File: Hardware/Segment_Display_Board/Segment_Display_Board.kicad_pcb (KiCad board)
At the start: 2 copper layers, 64.4 x 141 mm, 83 parts, among them J101 IN, J102 OUT, J301 USB_B_Micro, J302 PROG, J401 19V Input, J501 Bottom Conn, J502 Top Conn, Q1001 MMBT3904, Q1002 MMBT3906, Q1101 MMBT3904, Q1102 MMBT3906, Q1201 MMBT3904, Q1202 MMBT3906, Q601 MMBT3904, Q602 MMBT3906, Q701 MMBT3904, Q702 MMBT3906, Q801 MMBT3904, Q802 MMBT3906, Q901 MMBT3904, Q902 MMBT3906, SW201 RESET, SW202 DAY_RESET, SW203 DAY_ADV, SW204 DAY_SUB, U201 ATmega328P-A, U202 DS1307Z+, U301 FT232RL, U401 LM1117-5.0, U501 SN74HC595, Y201 16mHz, Y202 32.768kHz

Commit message: Steps for a RC1
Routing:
- net /USB/USB+: track 13.1 -> 15.1 mm
- net /USB/USB-: track 14.3 -> 15.2 mm

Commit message: Fix stuff i guess goodnight"
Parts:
- added JP501: SolderJumper_2_Bridged, Jumper:SolderJumper-2_P1.3mm_Bridged_Pad1.0x1.5mm, B.Cu at (166.5, 131.0)
- added JP502: SolderJumper_2_Bridged, Jumper:SolderJumper-2_P1.3mm_Bridged_Pad1.0x1.5mm, B.Cu at (166.5, 128.5)
- moved C303 0.50 mm to (121.5, 111.5)
- moved D302 0.25 mm to (115.0, 122.2)
- moved R302 0.25 mm to (118.5, 122.2)
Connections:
- net +3V3 renamed +3.3V
- J102 pad 3: /C_OUT -> /Display Card/CLOCK_OUT
- J102 pad 4: /L_OUT -> /Display Card/LATCH_OUT
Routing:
- net /L_OUT: track 99.1 -> 92.1 mm
- net /Display Card/LATCH_OUT: track 0.00 -> 6.40 mm
- net /Display Card/CLOCK_OUT: track 0.00 -> 6.36 mm
- net /C_OUT: track 92.7 -> 86.4 mm
- net VBUS: track 10.5 -> 10.00 mm
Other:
- board text added: "LCD Display Card ${FULL_REVISION}"
- board text removed: "LCD Display Card ${FULL_VERSION}"

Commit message: Add a bunch more great stuff
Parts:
- added G***: LOGO, 1721_templates:QRCODE_AccidentCounter, F.Cu at (122.5, 158.2)
- added REF**: OSHW-Symbol_13.4x12mm_SilkScreen, Symbol:OSHW-Symbol_13.4x12mm_SilkScreen, F.Cu at (124.2, 73.5)
- moved G*** 97.7 mm to (124.2, 59.0)
- moved D301 89.6 mm to (119.0, 35.0)
- moved D302 89.6 mm to (119.0, 32.8)
- moved R301 89.6 mm to (122.5, 35.0)
- moved R302 89.6 mm to (122.5, 32.8)
- moved C301 88.2 mm to (117.2, 40.0), turned to 180 degrees
- moved J301 83.5 mm to (131.2, 32.1), turned to 180 degrees
- moved C302 77.6 mm to (139.8, 32.0), turned to 0 degrees
- moved U301 77.5 mm to (124.2, 43.5), turned to 180 degrees
- moved C303 74.0 mm to (133.8, 38.5), turned to 0 degrees
- moved BT201 44.1 mm to (161.8, 50.5), turned to 90 degrees
- moved R205 30.6 mm to (144.8, 45.0), turned to 0 degrees
- moved R204 29.8 mm to (144.8, 43.0), turned to 0 degrees
- moved U202 28.2 mm to (140.8, 49.0), turned to 0 degrees
- moved Y202 28.2 mm to (144.2, 39.0), turned to 180 degrees
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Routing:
- net /MCU/RXD: track 14.7 -> 80.8 mm, vias 2 -> 3
- net /MCU/TXD: track 12.3 -> 77.5 mm
- net Net-(C304-Pad2): track 9.15 -> 73.1 mm
- net Net-(BT201-Pad1): track 36.4 -> 51.5 mm, vias 2 -> 4
- net +5V: track 303.3 -> 291.0 mm
- net +19V: track 215.8 -> 209.5 mm
- net /L_OUT: track 92.1 -> 86.1 mm
- net /D_OUT: track 82.8 -> 76.8 mm
- net /C_OUT: track 86.4 -> 80.3 mm
- net /MCU/SDA: track 72.7 -> 78.2 mm
- net /MCU/DAY_SUBTRACT: track 48.7 -> 54.2 mm
- net /MCU/DAY_ADVANCE: track 57.6 -> 63.0 mm
- net /MCU/DAY_RESET: track 64.6 -> 70.0 mm
- net GND: track 27.7 -> 22.9 mm
- net Net-(R302-Pad2): track 10.4 -> 14.3 mm
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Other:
- board size 64.4 x 141 mm -> 58.4 x 141 mm
- board text added: "Designed for FRC 1721 Tidal Force By Joe and Mark Sedutto"

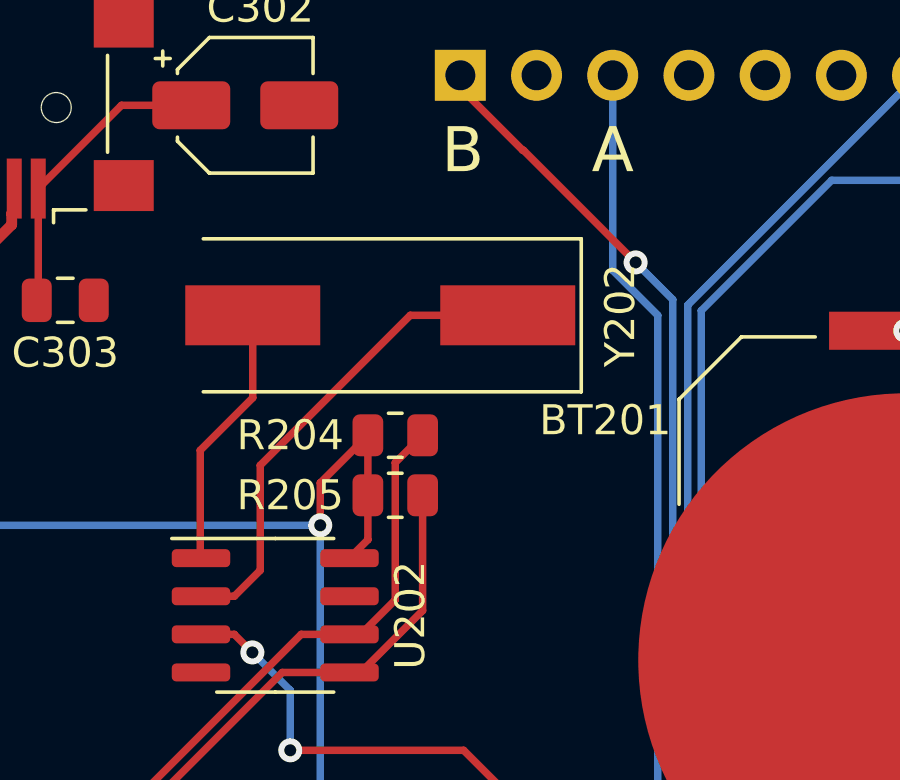
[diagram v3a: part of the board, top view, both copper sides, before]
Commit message: Place hardware orders
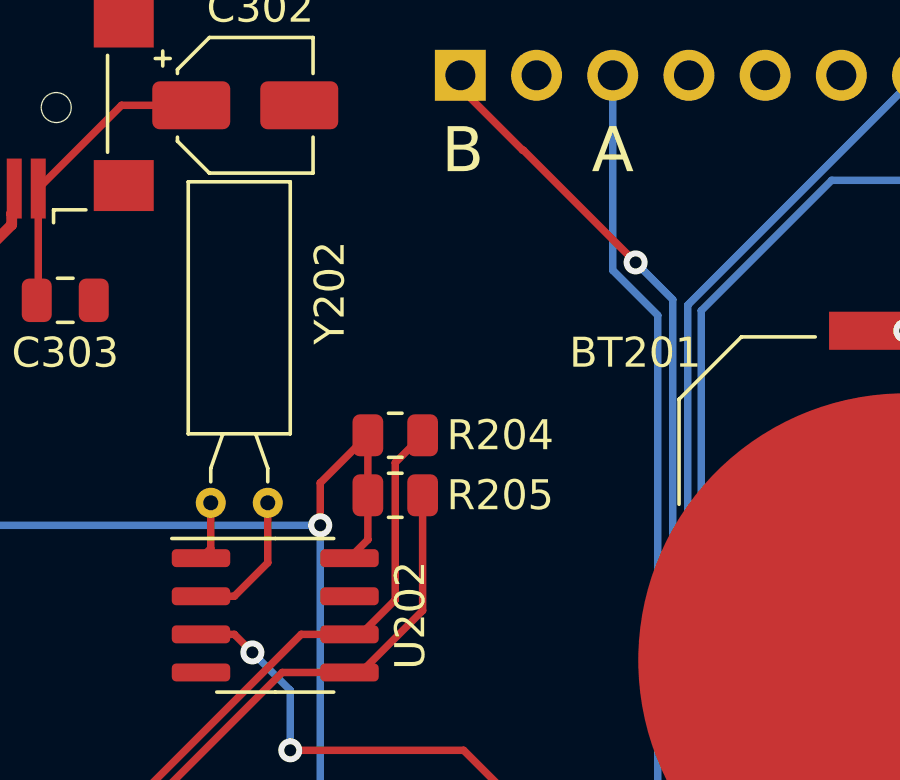
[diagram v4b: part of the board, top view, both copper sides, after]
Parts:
- R1003, R1103, R1203, R603, R703, R803, R903: value 250R -> 240R
- Y202: footprint Crystal:Crystal_SMD_HC49-SD -> Crystal:Crystal_C38-LF_D3.0mm_L8.0mm_Horizontal
- moved Y202 7.29 mm to (140.5, 45.2)
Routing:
- net Net-(U202-Pad2): track 16.2 -> 4.69 mm
- net Net-(U202-Pad1): track 8.83 -> 2.01 mm
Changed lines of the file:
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@@
       (effects (font (size 1 1) (thickness 0.15)))
     )
-    (fp_text value "4.7uf" (at 0 3.2) (layer "F.Fab")
+    (fp_text value "4.7uf" (at 4.5 1.75) (layer "F.Fab")
       (effects (font (size 1 1) (thickness 0.15)))
     )
@@
     (property "Sheetname" "MCU")
     (attr smd)
-    (fp_text reference "BT201" (at 8 -10) (layer "F.SilkS")
+    (fp_text reference "BT201" (at 10.25 -9) (layer "F.SilkS")
       (effects (font (size 1 1) (thickness 0.15)))
     )
@@
       (effects (font (size 0.75 0.75) (thickness 0.15)))
     )
-    (fp_text value "250R" (at 0 2.5) (layer "F.Fab")
+    (fp_text value "240R" (at 0 2.5) (layer "F.Fab")
       (effects (font (size 1 1) (thickness 0.15)))
     )
@@
     (property "Sheetname" "MCU")
     (attr smd)
-    (fp_text reference "R204" (at -3.5 0) (layer "F.SilkS")
+    (fp_text reference "R204" (at 3.5 0) (layer "F.SilkS")
       (effects (font (size 1 1) (thickness 0.15)))
     )
@@
       (effects (font (size 0.75 0.75) (thickness 0.15)))
     )
-    (fp_text value "250R" (at 0 2.5) (layer "F.Fab")
+    (fp_text value "240R" (at 0 2.5) (layer "F.Fab")
       (effects (font (size 1 1) (thickness 0.15)))
     )
@@
       (effects (font (size 0.75 0.75) (thickness 0.15)))
     )
-    (fp_text value "250R" (at 0 2.5) (layer "F.Fab")
+    (fp_text value "240R" (at 0 2.5) (layer "F.Fab")
       (effects (font (size 1 1) (thickness 0.15)))
     )
@@
       (effects (font (size 0.75 0.75) (thickness 0.15)))
     )
-    (fp_text value "250R" (at 0 2.5) (layer "F.Fab")
+    (fp_text value "240R" (at 0 2.5) (layer "F.Fab")
       (effects (font (size 1 1) (thickness 0.15)))
     )
@@
     (property "Sheetname" "MCU")
     (attr smd)
-    (fp_text reference "R205" (at -3.5 0) (layer "F.SilkS")
+    (fp_text reference "R205" (at 3.5 0) (layer "F.SilkS")
       (effects (font (size 1 1) (thickness 0.15)))
     )
@@
       (effects (font (size 0.75 0.75) (thickness 0.15)))
     )
-    (fp_text value "250R" (at 0 2.5) (layer "F.Fab")
+    (fp_text value "240R" (at 0 2.5) (layer "F.Fab")
       (effects (font (size 1 1) (thickness 0.15)))
     )
@@
       (effects (font (size 0.75 0.75) (thickness 0.15)))
     )
-    (fp_text value "250R" (at 0 2.5) (layer "F.Fab")
+    (fp_text value "240R" (at 0 2.5) (layer "F.Fab")
       (effects (font (size 1 1) (thickness 0.15)))
     )
@@
     )
   )
-  (footprint "Crystal:Crystal_SMD_HC49-SD" (layer "F.Cu")
-    (at 144.25 39 180)
-    (descr "SMD Crystal HC-49-SD http://cdn-reichelt.de/documents/datenblatt/B400/xxx-HC49-SMD.pdf, 11.4x4.7mm^2 package")
-    (tags "SMD SMT crystal")
+  (footprint "Crystal:Crystal_C38-LF_D3.0mm_L8.0mm_Horizontal" (layer "F.Cu")
+    (at 140.5 45.25 180)
+    (descr "Crystal THT C38-LF 8.0mm length 3.0mm diameter")
+    (tags "['C38-LF']")
     (property "Sheetfile" "mcu.kicad_sch")
     (property "Sheetname" "MCU")
-    (attr smd)
-    (fp_text reference "Y202" (at -8 0 90) (layer "F.SilkS")
+    (attr through_hole)
+    (fp_text reference "Y202" (at -2.07 7 270) (layer "F.SilkS")
       (effects (font (size 1 1) (thickness 0.15)))
     )
-    (fp_text value "32.768kHz" (at -1.75 3.25) (layer "F.Fab")
+    (fp_text value "32.768kHz" (at 1 6.5 270) (layer "F.Fab")
       (effects (font (size 1 1) (thickness 0.15)))
     )
-    (fp_text user "${REFERENCE}" (at 0 0) (layer "F.Fab")
-      (effects (font (size 1 1) (thickness 0.15)))
+    (fp_text user "${REFERENCE}" (at 1.25 6.5 270) (layer "F.Fab")
+      (effects (font (size 0.7 0.7) (thickness 0.105)))
     )
-    (fp_line (start -6.7 2.55) (end 5.9 2.55) (layer "F.SilkS") (width 0.12))
-    (fp_line (start -6.7 -2.55) (end -6.7 2.55) (layer "F.SilkS") (width 0.12))
-    (fp_line (start 5.9 -2.55) (end -6.7 -2.55) (layer "F.SilkS") (width 0.12))
-    (fp_line (start -6.8 2.6) (end 6.8 2.6) (layer "F.CrtYd") (width 0.05))
-    (fp_line (start -6.8 -2.6) (end -6.8 2.6) (layer "F.CrtYd") (width 0.05))
-    (fp_line (start 6.8 2.6) (end 6.8 -2.6) (layer "F.CrtYd") (width 0.05))
-    (fp_line (start 6.8 -2.6) (end -6.8 -2.6) (layer "F.CrtYd") (width 0.05))
-    (fp_line (start -3.015 2.115) (end 3.015 2.115) (layer "F.Fab") (width 0.1))
-    (fp_line (start 5.7 2.35) (end 5.7 -2.35) (layer "F.Fab") (width 0.1))
-    (fp_line (start -5.7 2.35) (end 5.7 2.35) (layer "F.Fab") (width 0.1))
-    (fp_line (start -5.7 -2.35) (end -5.7 2.35) (layer "F.Fab") (width 0.1))
-    (fp_line (start -3.015 -2.115) (end 3.015 -2.115) (layer "F.Fab") (width 0.1))
-    (fp_line (start 5.7 -2.35) (end -5.7 -2.35) (layer "F.Fab") (width 0.1))
-    (fp_arc (start 3.015 -2.115) (mid 5.13 0) (end 3.015 2.115) (layer "F.Fab") (width 0.1))
-    (fp_arc (start -3.015 2.115) (mid -5.13 0) (end -3.015 -2.115) (layer "F.Fab") (width 0.1))
-    (pad "1" smd rect (at -4.25 0 180) (size 4.5 2) (layers "F.Cu" "F.Paste" "F.Mask")
+    (fp_line (start -0.75 2.3) (end -0.75 10.7) (layer "F.SilkS") (width 0.12))
+    (fp_line (start 1.495 2.3) (end 1.9 1.15) (layer "F.SilkS") (width 0.12))
+    (fp_line (start 2.65 10.7) (end 2.65 2.3) (layer "F.SilkS") (width 0.12))
+    (fp_line (start 0.405 2.3) (end 0 1.15) (layer "F.SilkS") (width 0.12))
+    (fp_line (start 2.65 2.3) (end -0.75 2.3) (layer "F.SilkS") (width 0.12))
+    (fp_line (start 1.9 1.15) (end 1.9 0.7) (layer "F.SilkS") (width 0.12))
+    (fp_line (start 0 1.15) (end 0 0.7) (layer "F.SilkS") (width 0.12))
+    (fp_line (start -0.75 10.7) (end 2.65 10.7) (layer "F.SilkS") (width 0.12))
+    (fp_line (start 3.2 11.3) (end 3.2 -0.8) (layer "F.CrtYd") (width 0.05))
+    (fp_line (start -1.3 -0.8) (end -1.3 11.3) (layer "F.CrtYd") (width 0.05))
+    (fp_line (start 3.2 -0.8) (end -1.3 -0.8) (layer "F.CrtYd") (width 0.05))
+    (fp_line (start -1.3 11.3) (end 3.2 11.3) (layer "F.CrtYd") (width 0.05))
+    (fp_line (start 1.9 1.25) (end 1.9 0) (layer "F.Fab") (width 0.1))
+    (fp_line (start 0 1.25) (end 0 0) (layer "F.Fab") (width 0.1))
+    (fp_line (start 1.495 2.5) (end 1.9 1.25) (layer "F.Fab") (width 0.1))
+    (fp_line (start 2.45 2.5) (end -0.55 2.5) (layer "F.Fab") (width 0.1))
+    (fp_line (start -0.55 10.5) (end 2.45 10.5) (layer "F.Fab") (width 0.1))
+    (fp_line (start 0.405 2.5) (end 0 1.25) (layer "F.Fab") (width 0.1))
+    (fp_line (start -0.55 2.5) (end -0.55 10.5) (layer "F.Fab") (width 0.1))
+    (fp_line (start 2.45 10.5) (end 2.45 2.5) (layer "F.Fab") (width 0.1))
+    (pad "1" thru_hole circle (at 0 0 180) (size 1 1) (drill 0.5) (layers *.Cu *.Mask)
       (net 66 "Net-(U202-Pad2)") (pinfunction "1") (pintype "passive"))
-    (pad "2" smd rect (at 4.25 0 180) (size 4.5 2) (layers "F.Cu" "F.Paste" "F.Mask")
+    (pad "2" thru_hole circle (at 1.9 0 180) (size 1 1) (drill 0.5) (layers *.Cu *.Mask)
       (net 65 "Net-(U202-Pad1)") (pinfunction "2") (pintype "passive"))
-    (model "${KICAD6_3DMODEL_DIR}/Crystal.3dshapes/Crystal_SMD_HC49-SD.wrl"
+    (model "${KICAD6_3DMODEL_DIR}/Crystal.3dshapes/Crystal_C38-LF_D3.0mm_L8.0mm_Horizontal.wrl"
       (offset (xyz 0 0 0))
       (scale (xyz 1 1 1))
@@
       (effects (font (size 0.75 0.75) (thickness 0.15)))
     )
-    (fp_text value "250R" (at 0 2.5) (layer "F.Fab")
+    (fp_text value "240R" (at 0 2.5) (layer "F.Fab")
       (effects (font (size 1 1) (thickness 0.15)))
     )
@@
   (segment (start 133.5 108) (end 133.5 104.5) (width 0.25) (layer "F.Cu") (net 64))
   (segment (start 143.601751 50.905) (end 143.225 50.905) (width 0.25) (layer "F.Cu") (net 64))
-  (segment (start 140 41.75) (end 138.25 43.5) (width 0.25) (layer "F.Cu") (net 65))
   (segment (start 138.25 47.07) (end 138.275 47.095) (width 0.25) (layer "F.Cu") (net 65))
-  (segment (start 140 39) (end 140 41.75) (width 0.25) (layer "F.Cu") (net 65))
-  (segment (start 138.25 43.5) (end 138.25 47.07) (width 0.25) (layer "F.Cu") (net 65))
-  (segment (start 140.25 47.5) (end 140.25 44) (width 0.25) (layer "F.Cu") (net 66))
-  (segment (start 140.25 44) (end 145.25 39) (width 0.25) (layer "F.Cu") (net 66))
-  (segment (start 138.275 48.365) (end 139.385 48.365) (width 0.25) (layer "F.Cu") (net 66))
-  (segment (start 139.385 48.365) (end 140.25 47.5) (width 0.25) (layer "F.Cu") (net 66))
-  (segment (start 145.25 39) (end 148.5 39) (width 0.25) (layer "F.Cu") (net 66))
+  (segment (start 138.6 46.77) (end 138.6 45.25) (width 0.25) (layer "F.Cu") (net 65))
+  (segment (start 138.275 47.095) (end 138.6 46.77) (width 0.25) (layer "F.Cu") (net 65))
+  (segment (start 140.5 45.25) (end 140.5 47.25) (width 0.25) (layer "F.Cu") (net 66))
+  (segment (start 139.385 48.365) (end 138.275 48.365) (width 0.25) (layer "F.Cu") (net 66))
+  (segment (start 140.5 47.25) (end 139.385 48.365) (width 0.25) (layer "F.Cu") (net 66))
   (segment (start 124.5 106.38) (end 126.93 106.38) (width 0.25) (layer "F.Cu") (net 69))
   (segment (start 126.93 106.38) (end 127.05 106.5) (width 0.25) (layer "F.Cu") (net 69))

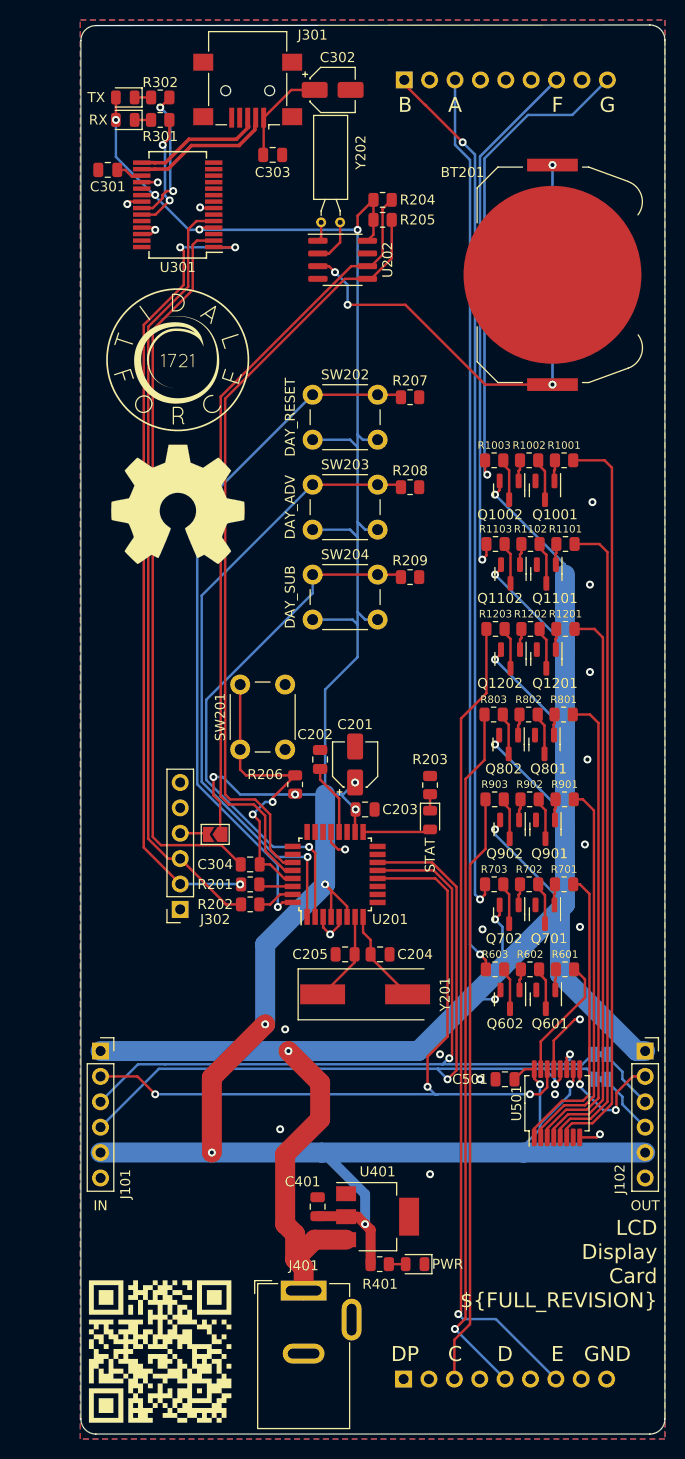
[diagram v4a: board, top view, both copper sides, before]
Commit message: Add a nice outline so you know what a client brd needs
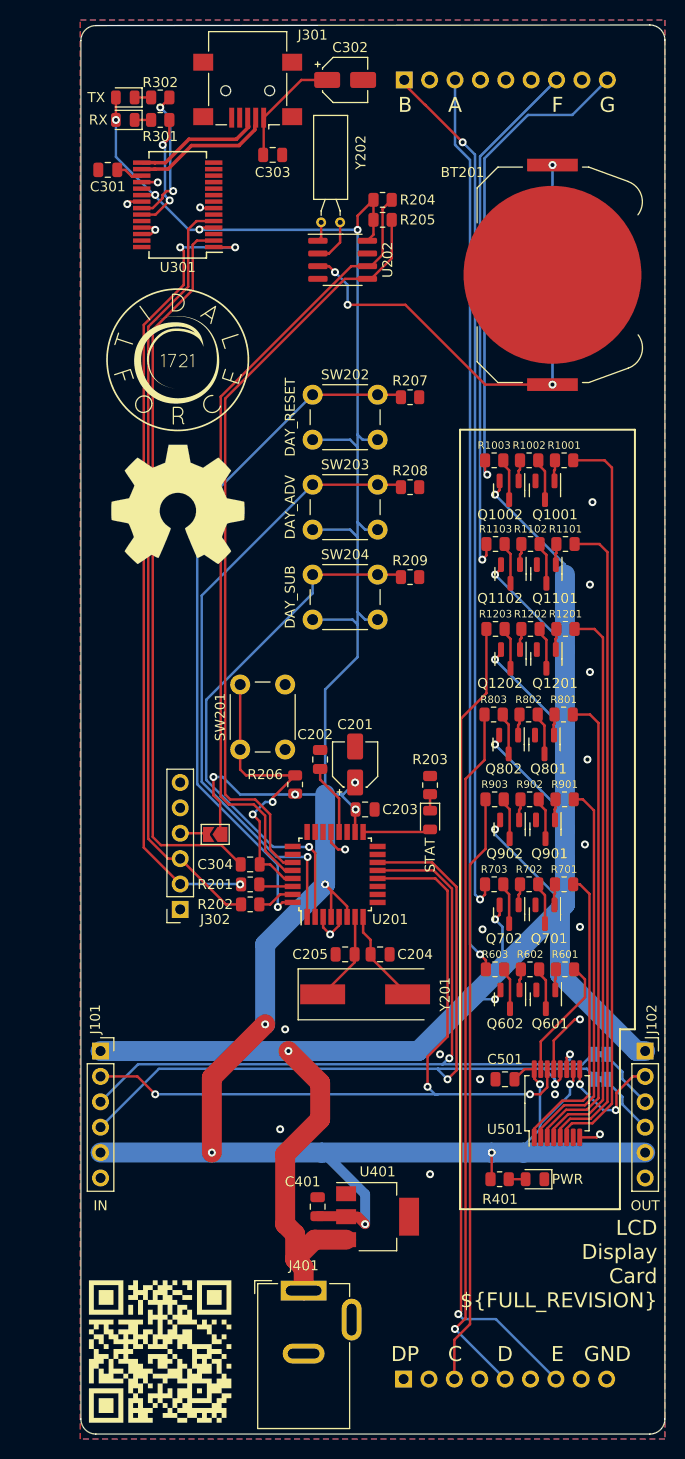
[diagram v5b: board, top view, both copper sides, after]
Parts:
- moved D401 14.7 mm to (160.0, 141.0)
- moved R401 14.7 mm to (156.5, 141.0)
- moved C302 1.60 mm to (141.0, 31.0)
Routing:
- net VBUS: track 10.00 -> 11.7 mm
- net +5V: track 291.0 -> 289.5 mm, vias 14 -> 15

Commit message: Use a different regulator
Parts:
- U401: value LM1117-5.0 -> NCV1117ST50T3G
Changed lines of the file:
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@@
       (effects (font (size 1 1) (thickness 0.15)))
     )
-    (fp_text value "LM1117-5.0" (at 0 4.5) (layer "F.Fab") hide
+    (fp_text value "NCV1117ST50T3G" (at 0 4.5) (layer "F.Fab") hide
       (effects (font (size 1 1) (thickness 0.15)))
     )

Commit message: include fixups fro EE
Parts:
- removed the C201 at (142.0, 99.5)
- added C401: 10uf, Capacitor_SMD:CP_Elec_4x3, F.Cu at (131.2, 147.0)
- added C402: 100nF, Capacitor_SMD:C_0805_2012Metric, F.Cu at (132.0, 143.0)
- added C404: 1uf, Capacitor_SMD:CP_Elec_4x3, F.Cu at (148.0, 152.0)
- added R301: 4K7, Resistor_SMD:R_0805_2012Metric, F.Cu at (135.0, 40.5)
- added R302: 10K, Resistor_SMD:R_0805_2012Metric, F.Cu at (131.5, 40.5)
- C302: value 4.7uf -> 100nF; footprint Capacitor_SMD:CP_Elec_4x3 -> Capacitor_SMD:C_0805_2012Metric
- C303: value 100nf -> 100nF
- C501: value 10uF -> 100nF
- moved C302 26.9 mm to (117.5, 44.0), turned to -90 degrees
- moved C303 7.55 mm to (130.0, 45.0), turned to 90 degrees
- renumbered C202 to C201, C203 to C202, C204 to C203, C205 to C204, C401 to C403, R301 to R303, R302 to R304
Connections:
- C302 pad 1: VBUS -> +5V
- C303 pad 1: VBUS -> +5V
- U301 pad 19: unconnected-(U301-Pad19) -> Net-(R301-Pad1)
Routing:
- net Net-(R301-Pad1): track 0.00 -> 14.0 mm, vias 0 -> 2
- net +5V: track 289.5 -> 298.6 mm, vias 15 -> 14
- net VBUS: track 11.7 -> 6.99 mm
- net +19V: track 209.5 -> 213.5 mm

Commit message: Add stencil and small text fixup
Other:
- board text added: "Segment Display Card ${FULL_REVISION}"
- board text removed: "LCD Display Card ${FULL_REVISION}"
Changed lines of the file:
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@@
     (effects (font (size 1.5 1.5) (thickness 0.3)))
   )
-  (gr_text "LCD\nDisplay\nCard\n${FULL_REVISION}" (at 172.25 149.5) (layer "F.SilkS")
+  (gr_text "Segment\nDisplay\nCard\n${FULL_REVISION}" (at 172.25 149.5) (layer "F.SilkS")
     (effects (font (size 1.5 1.5) (thickness 0.3)) (justify right))
   )
